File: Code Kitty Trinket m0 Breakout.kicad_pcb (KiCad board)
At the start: 2 copper layers, 39.6 x 39.6 mm, 9 parts, among them J1 Power, J2 Touch, P1 Left Servo, P2 Right Servo, P3 Sensor

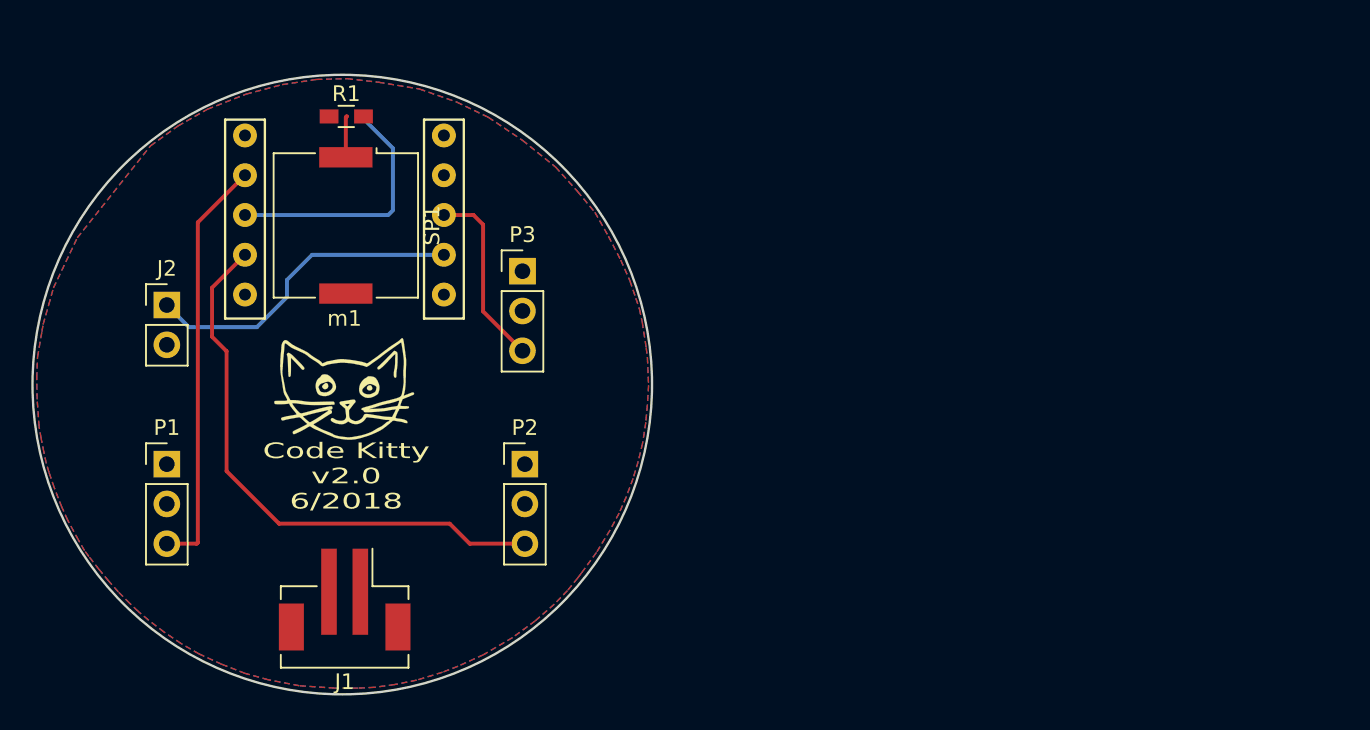
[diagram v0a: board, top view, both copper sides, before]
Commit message: Version 2.1 redesign
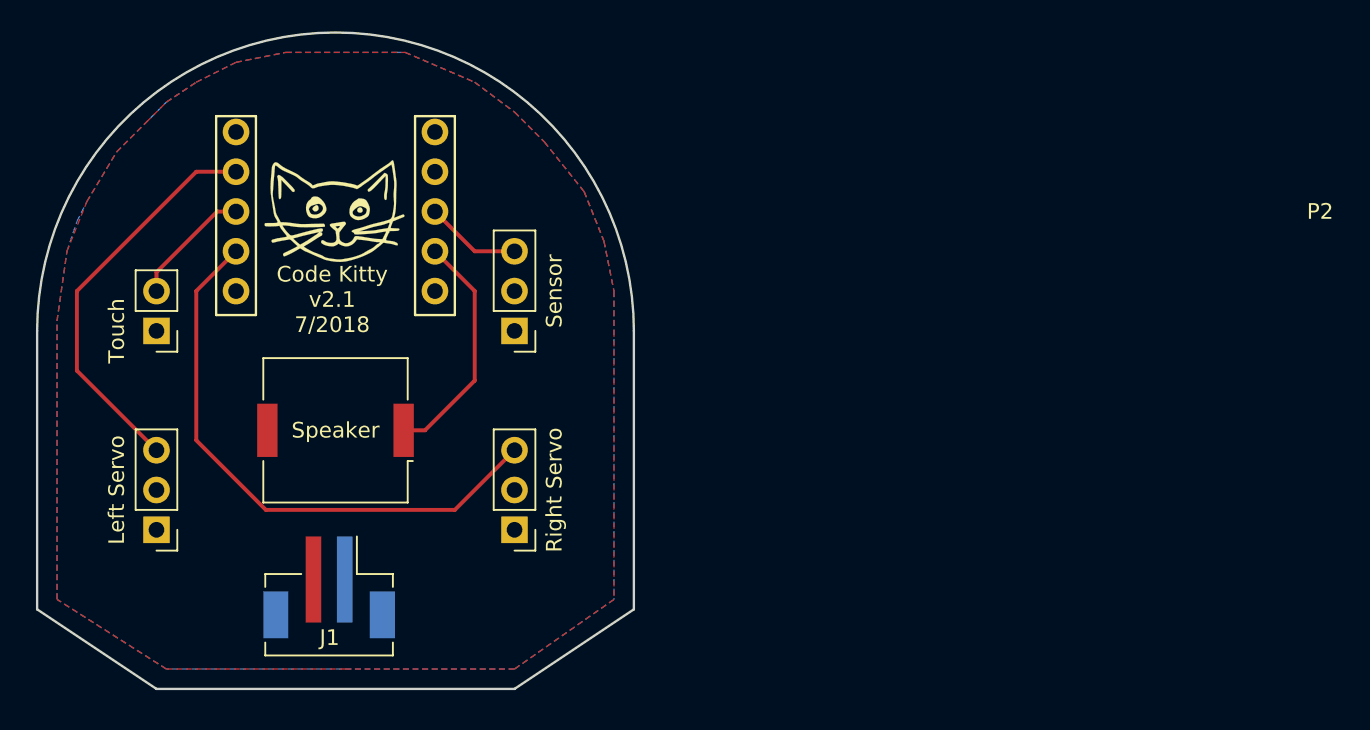
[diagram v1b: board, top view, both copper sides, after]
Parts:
- removed R1: 1K, Resistors_SMD:R_0603_HandSoldering
- m1: value (none) -> Trinket-m0
- moved Speaker 13.1 mm to (156.2, 133.3), turned to 180 degrees
- moved G*** 11.4 mm to (156.0, 119.4)
- moved P1 4.24 mm to (144.8, 139.7), turned to 180 degrees
- moved P2 4.24 mm to (167.6, 139.7), turned to 180 degrees
- moved P3 3.84 mm to (167.6, 127.0), turned to 180 degrees
- moved P4 1.78 mm to (144.8, 127.0), turned to 180 degrees
- moved J1 1.26 mm to (155.8, 144.0)
- moved m1 0.61 mm to (148.6, 105.7)
- renumbered J2 to P4, SP1 to Speaker
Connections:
- J1 pad : (no net) -> GND
- J1 pad 1: VCC -> GND
- J1 pad 2: GND -> VCC
- P4 pad 1: Touch -> GND
- P4 pad 2: GND -> Touch
- Speaker pad 1: Net-(R1-Pad1) -> BUZZ
- m1 pad 10: Net-(m1-Pad10) -> (no net)
- m1 pad 4: Touch -> BUZZ
- m1 pad 5: Net-(m1-Pad5) -> (no net)
- m1 pad 6: Net-(m1-Pad6) -> VCC
- m1 pad 8: BUZZ -> Touch
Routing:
- net Touch: track 21.4 -> 7.89 mm
- net SENS: track 11.9 -> 6.13 mm
- net Net-(R1-Pad1): track 2.66 -> 0.00 mm
- net LSERVO: track 26.7 -> 25.6 mm
- net BUZZ: track 16.1 -> 15.2 mm
- net RSERVO: track 36.0 -> 36.9 mm
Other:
- board size 39.6 x 39.6 mm -> 38.1 x 41.9 mm
- rule pad_to_mask_clearance: 0.2 -> 0.0508
- board text added: "Code Kitty v2.1 7/2018"
- board text added: "Left Servo"
- board text added: "Right Servo"
- board text added: "Sensor"
- board text added: "Touch"
- board text removed: "Code Kitty v2.0 6/2018"

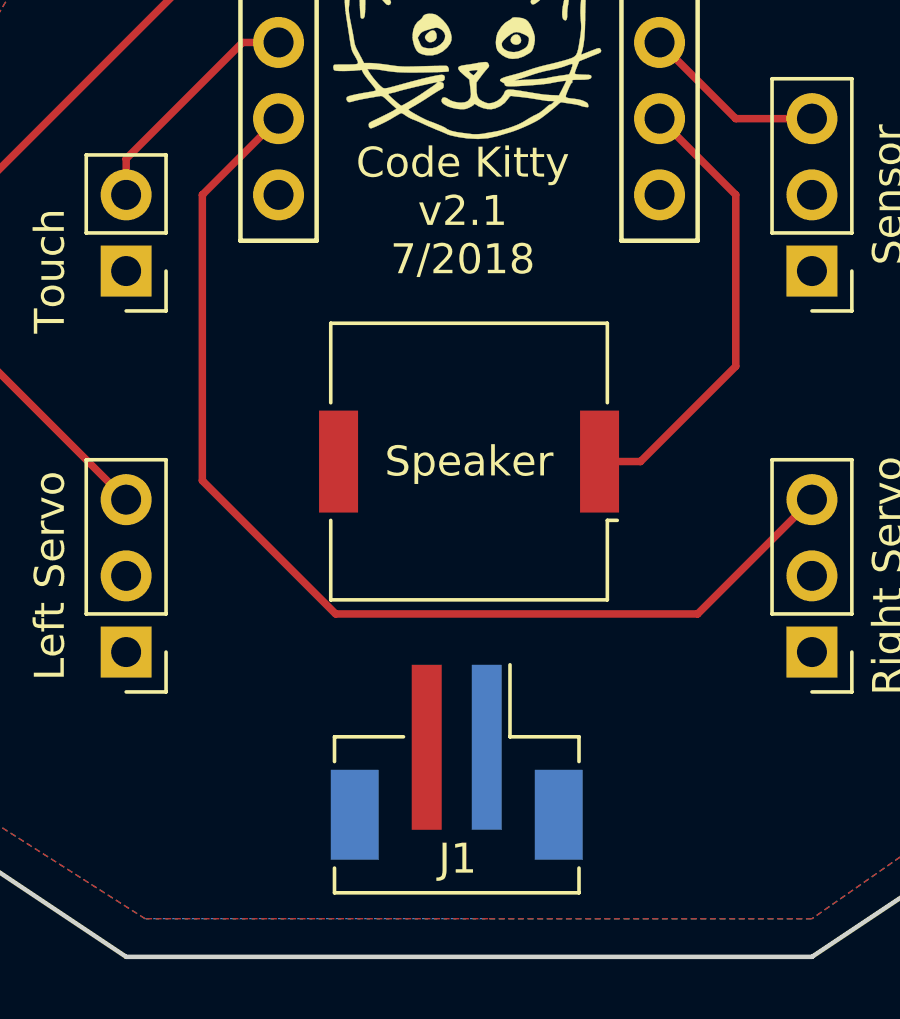
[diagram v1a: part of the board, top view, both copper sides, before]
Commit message: added ground vias for JST connector and Speaker
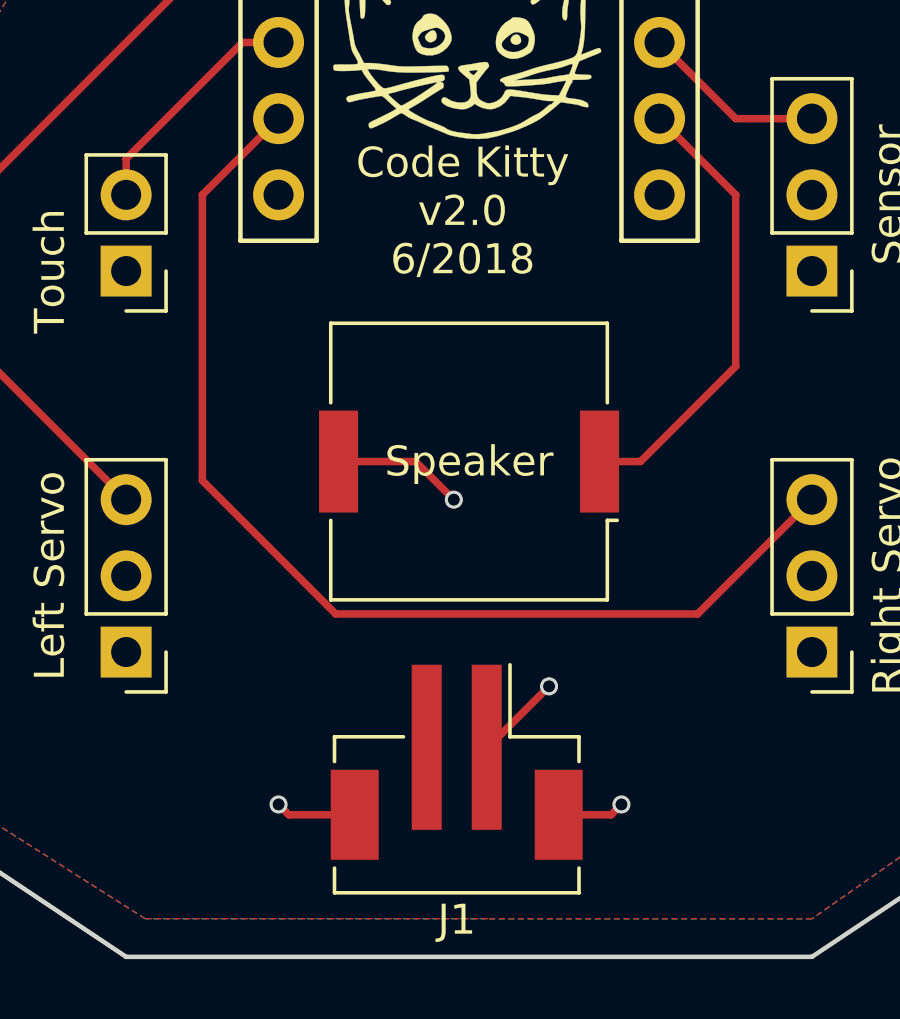
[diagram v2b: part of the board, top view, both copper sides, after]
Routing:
- net GND: track 0.00 -> 12.2 mm, vias 0 -> 4
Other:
- board text added: "Code Kitty v2.0 6/2018"
- board text removed: "Code Kitty v2.1 7/2018"
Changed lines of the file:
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@@
   (general
     (links 18)
-    (no_connects 1)
+    (no_connects 0)
     (area 137.084999 105.22 220.251191 149.935001)
     (thickness 1.6)
     (drawings 11)
-    (tracks 19)
+    (tracks 31)
     (zones 0)
     (modules 8)
@@
   (layers
     (0 F.Cu signal)
-    (31 B.Cu signal)
+    (31 B.Cu signal hide)
     (32 B.Adhes user)
     (33 F.Adhes user)
@@
   (setup
     (last_trace_width 0.25)
+    (user_trace_width 0.5)
     (trace_clearance 0.2)
     (zone_clearance 0.508)
@@
     (add_net Touch)
     (add_net VCC)
-  )
-  (module Connectors_JST:JST_PH_B2B-PH-SM4-TB_02x2.00mm_Straight (layer F.Cu)
-    (at 155.8 144 180)
-    (descr "JST PH series connector, B2B-PH-SM4-TB, top entry type, surface mount, Datasheet: http://www.jst-mfg.com/product/pdf/eng/ePH.pdf")
-    (tags "connector jst ph")
-    (attr smd)
-    (fp_text reference J1 (at -0.03 -2.59 180) (layer F.SilkS)
-      (effects (font (size 1 1) (thickness 0.15)))
-    )
-    (fp_text value Power (at 0 4.875 180) (layer F.Fab)
-      (effects (font (size 1 1) (thickness 0.15)))
-    )
-    (fp_line (start -4.075 -2.9) (end -4.075 -3.725) (layer F.SilkS) (width 0.12))
-    (fp_line (start -4.075 -3.725) (end 4.075 -3.725) (layer F.SilkS) (width 0.12))
-    (fp_line (start 4.075 -3.725) (end 4.075 -2.9) (layer F.SilkS) (width 0.12))
-    (fp_line (start -4.075 0.65) (end -4.075 1.475) (layer F.SilkS) (width 0.12))
-    (fp_line (start -4.075 1.475) (end -1.775 1.475) (layer F.SilkS) (width 0.12))
-    (fp_line (start 4.075 0.65) (end 4.075 1.475) (layer F.SilkS) (width 0.12))
-    (fp_line (start 4.075 1.475) (end 1.775 1.475) (layer F.SilkS) (width 0.12))
-    (fp_line (start -3.975 -3.625) (end -3.975 1.375) (layer F.Fab) (width 0.1))
-    (fp_line (start -3.975 1.375) (end 3.975 1.375) (layer F.Fab) (width 0.1))
-    (fp_line (start 3.975 1.375) (end 3.975 -3.625) (layer F.Fab) (width 0.1))
-    (fp_line (start 3.975 -3.625) (end -3.975 -3.625) (layer F.Fab) (width 0.1))
-    (fp_line (start -1.775 1.475) (end -1.775 3.875) (layer F.SilkS) (width 0.12))
-    (fp_line (start -2 1.375) (end -1 0.375) (layer F.Fab) (width 0.1))
-    (fp_line (start -1 0.375) (end 0 1.375) (layer F.Fab) (width 0.1))
-    (fp_line (start -4.7 -4.13) (end -4.7 4.38) (layer F.CrtYd) (width 0.05))
-    (fp_line (start -4.7 4.38) (end 4.7 4.38) (layer F.CrtYd) (width 0.05))
-    (fp_line (start 4.7 4.38) (end 4.7 -4.13) (layer F.CrtYd) (width 0.05))
-    (fp_line (start 4.7 -4.13) (end -4.7 -4.13) (layer F.CrtYd) (width 0.05))
-    (fp_text user %R (at 0 -2.625 180) (layer F.Fab)
-      (effects (font (size 1 1) (thickness 0.15)))
-    )
-    (pad 1 smd rect (at -1 1.125 180) (size 1 5.5) (layers B.Cu F.Paste F.Mask)
-      (net 2 GND))
-    (pad 2 smd rect (at 1 1.125 180) (size 1 5.5) (layers F.Cu F.Paste F.Mask)
-      (net 1 VCC))
-    (pad "" smd rect (at -3.4 -1.125 180) (size 1.6 3) (layers B.Cu F.Paste F.Mask)
-      (net 2 GND))
-    (pad "" smd rect (at 3.4 -1.125 180) (size 1.6 3) (layers B.Cu F.Paste F.Mask)
-      (net 2 GND))
-    (model ${KISYS3DMOD}/Connectors_JST.3dshapes/JST_PH_B2B-PH-SM4-TB_02x2.00mm_Straight.wrl
-      (at (xyz 0 0 0))
-      (scale (xyz 1 1 1))
-      (rotate (xyz 0 0 0))
-    )
   )
   (module Buzzers_Beepers:Buzzer_Murata_PKMCS0909E4000-R1 (layer F.Cu)
@@
       (xy -1.172602 -0.309545) (xy -1.077038 -0.381913) (xy -0.997162 -0.406855) (xy -0.934043 -0.384502)) (layer F.SilkS) (width 0.01))
   )
+  (module Connectors_JST:JST_PH_B2B-PH-SM4-TB_02x2.00mm_Straight (layer F.Cu)
+    (at 155.8 144 180)
+    (descr "JST PH series connector, B2B-PH-SM4-TB, top entry type, surface mount, Datasheet: http://www.jst-mfg.com/product/pdf/eng/ePH.pdf")
+    (tags "connector jst ph")
+    (attr smd)
+    (fp_text reference J1 (at 0 -4.625 180) (layer F.SilkS)
+      (effects (font (size 1 1) (thickness 0.15)))
+    )
+    (fp_text value Power (at 0 4.875 180) (layer F.Fab)
+      (effects (font (size 1 1) (thickness 0.15)))
+    )
+    (fp_line (start -4.075 -2.9) (end -4.075 -3.725) (layer F.SilkS) (width 0.12))
+    (fp_line (start -4.075 -3.725) (end 4.075 -3.725) (layer F.SilkS) (width 0.12))
+    (fp_line (start 4.075 -3.725) (end 4.075 -2.9) (layer F.SilkS) (width 0.12))
+    (fp_line (start -4.075 0.65) (end -4.075 1.475) (layer F.SilkS) (width 0.12))
+    (fp_line (start -4.075 1.475) (end -1.775 1.475) (layer F.SilkS) (width 0.12))
+    (fp_line (start 4.075 0.65) (end 4.075 1.475) (layer F.SilkS) (width 0.12))
+    (fp_line (start 4.075 1.475) (end 1.775 1.475) (layer F.SilkS) (width 0.12))
+    (fp_line (start -3.975 -3.625) (end -3.975 1.375) (layer F.Fab) (width 0.1))
+    (fp_line (start -3.975 1.375) (end 3.975 1.375) (layer F.Fab) (width 0.1))
+    (fp_line (start 3.975 1.375) (end 3.975 -3.625) (layer F.Fab) (width 0.1))
+    (fp_line (start 3.975 -3.625) (end -3.975 -3.625) (layer F.Fab) (width 0.1))
+    (fp_line (start -1.775 1.475) (end -1.775 3.875) (layer F.SilkS) (width 0.12))
+    (fp_line (start -2 1.375) (end -1 0.375) (layer F.Fab) (width 0.1))
+    (fp_line (start -1 0.375) (end 0 1.375) (layer F.Fab) (width 0.1))
+    (fp_line (start -4.7 -4.13) (end -4.7 4.38) (layer F.CrtYd) (width 0.05))
+    (fp_line (start -4.7 4.38) (end 4.7 4.38) (layer F.CrtYd) (width 0.05))
+    (fp_line (start 4.7 4.38) (end 4.7 -4.13) (layer F.CrtYd) (width 0.05))
+    (fp_line (start 4.7 -4.13) (end -4.7 -4.13) (layer F.CrtYd) (width 0.05))
+    (fp_text user %R (at 0 -2.625 180) (layer F.Fab)
+      (effects (font (size 1 1) (thickness 0.15)))
+    )
+    (pad 1 smd rect (at -1 1.125 180) (size 1 5.5) (layers F.Cu F.Paste F.Mask)
+      (net 2 GND))
+    (pad 2 smd rect (at 1 1.125 180) (size 1 5.5) (layers F.Cu F.Paste F.Mask)
+      (net 1 VCC))
+    (pad "" smd rect (at -3.4 -1.125 180) (size 1.6 3) (layers F.Cu F.Paste F.Mask)
+      (net 2 GND))
+    (pad "" smd rect (at 3.4 -1.125 180) (size 1.6 3) (layers F.Cu F.Paste F.Mask)
+      (net 2 GND))
+    (model ${KISYS3DMOD}/Connectors_JST.3dshapes/JST_PH_B2B-PH-SM4-TB_02x2.00mm_Straight.wrl
+      (at (xyz 0 0 0))
+      (scale (xyz 1 1 1))
+      (rotate (xyz 0 0 0))
+    )
+  )
   (gr_line (start 144.78 149.86) (end 137.16 144.78) (layer Edge.Cuts) (width 0.15))
   (gr_line (start 167.64 149.86) (end 144.78 149.86) (layer Edge.Cuts) (width 0.15))
@@
     (effects (font (size 1 1) (thickness 0.25)))
   )
-  (gr_text "Code Kitty\nv2.1\n7/2018" (at 156 125) (layer F.SilkS)
+  (gr_text "Code Kitty\nv2.0\n6/2018" (at 156 125) (layer F.SilkS)
     (effects (font (size 1 1) (thickness 0.1)))
   )
   (segment (start 163.1315 114.5226) (end 163.2144 114.5226) (width 0.25) (layer F.Cu) (net 1) (status 30))
+  (segment (start 151.86 133.35) (end 154.432 133.35) (width 0.25) (layer F.Cu) (net 2) (status 400000))
+  (via (at 155.702 134.62) (size 0.6) (drill 0.4) (layers F.Cu B.Cu) (net 2))
+  (segment (start 154.432 133.35) (end 155.702 134.62) (width 0.25) (layer F.Cu) (net 2))
+  (via (at 158.877 140.843) (size 0.6) (drill 0.4) (layers F.Cu B.Cu) (net 2))
+  (segment (start 156.845 142.875) (end 158.877 140.843) (width 0.25) (layer F.Cu) (net 2) (status 400000))
+  (segment (start 156.8 142.875) (end 156.845 142.875) (width 0.25) (layer F.Cu) (net 2) (status C00000))
+  (segment (start 159.2 145.125) (end 160.945 145.125) (width 0.25) (layer F.Cu) (net 2) (status 400000))
+  (via (at 161.29 144.78) (size 0.6) (drill 0.4) (layers F.Cu B.Cu) (net 2))
+  (segment (start 160.945 145.125) (end 161.29 144.78) (width 0.25) (layer F.Cu) (net 2))
+  (segment (start 152.4 145.125) (end 150.205 145.125) (width 0.25) (layer F.Cu) (net 2) (status 400000))
+  (via (at 149.86 144.78) (size 0.6) (drill 0.4) (layers F.Cu B.Cu) (net 2))
+  (segment (start 150.205 145.125) (end 149.86 144.78) (width 0.25) (layer F.Cu) (net 2))
   (segment (start 149.86 119.38) (end 148.657919 119.38) (width 0.25) (layer F.Cu) (net 3))
   (segment (start 148.657919 119.38) (end 144.78 123.257919) (width 0.25) (layer F.Cu) (net 3))

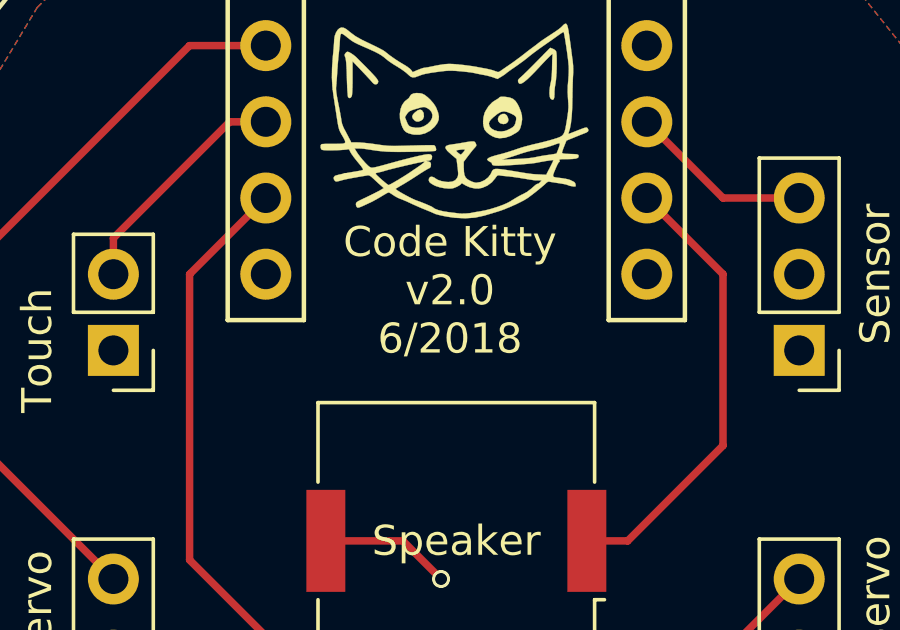
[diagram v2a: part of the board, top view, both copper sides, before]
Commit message: Fixed text on board to say Code Kitty 2.2
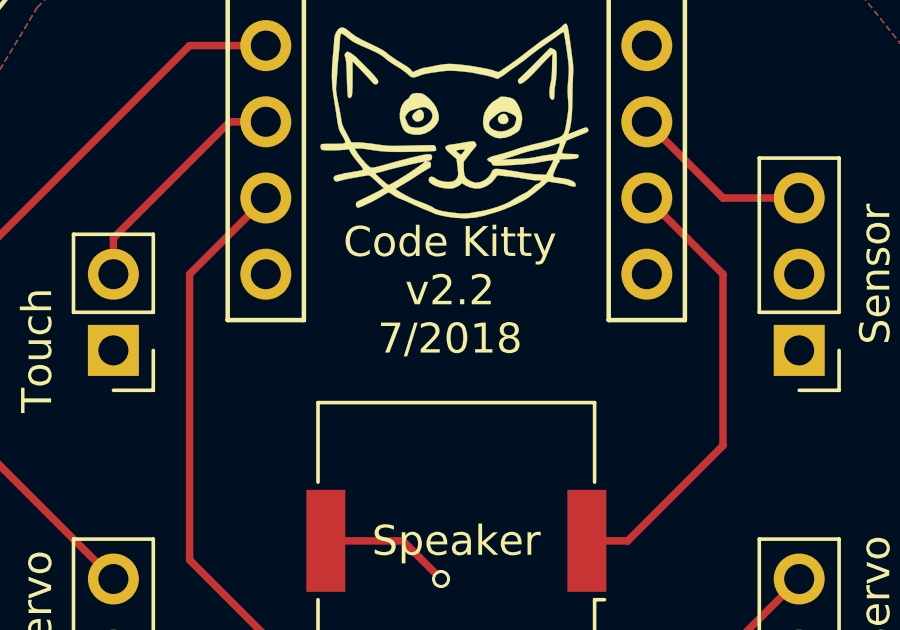
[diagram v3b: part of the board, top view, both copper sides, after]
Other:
- board text added: "Code Kitty v2.2 7/2018"
- board text removed: "Code Kitty v2.0 6/2018"
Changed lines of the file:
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@@
     (links 18)
     (no_connects 0)
-    (area 137.084999 105.22 220.251191 149.935001)
+    (area 137.084999 107.874999 175.335001 149.935001)
     (thickness 1.6)
     (drawings 11)
@@
     (effects (font (size 1 1) (thickness 0.25)))
   )
-  (gr_text "Code Kitty\nv2.0\n6/2018" (at 156 125) (layer F.SilkS)
+  (gr_text "Code Kitty\nv2.2\n7/2018" (at 156 125) (layer F.SilkS)
     (effects (font (size 1 1) (thickness 0.1)))
   )
   (segment (start 163.1315 114.5226) (end 163.2144 114.5226) (width 0.25) (layer F.Cu) (net 1) (status 30))
-  (segment (start 151.86 133.35) (end 154.432 133.35) (width 0.25) (layer F.Cu) (net 2) (status 400000))
+  (segment (start 151.86 133.35) (end 154.432 133.35) (width 0.25) (layer F.Cu) (net 2))
   (via (at 155.702 134.62) (size 0.6) (drill 0.4) (layers F.Cu B.Cu) (net 2))
   (segment (start 154.432 133.35) (end 155.702 134.62) (width 0.25) (layer F.Cu) (net 2))
   (via (at 158.877 140.843) (size 0.6) (drill 0.4) (layers F.Cu B.Cu) (net 2))
-  (segment (start 156.845 142.875) (end 158.877 140.843) (width 0.25) (layer F.Cu) (net 2) (status 400000))
-  (segment (start 156.8 142.875) (end 156.845 142.875) (width 0.25) (layer F.Cu) (net 2) (status C00000))
-  (segment (start 159.2 145.125) (end 160.945 145.125) (width 0.25) (layer F.Cu) (net 2) (status 400000))
+  (segment (start 156.845 142.875) (end 158.877 140.843) (width 0.25) (layer F.Cu) (net 2))
+  (segment (start 156.8 142.875) (end 156.845 142.875) (width 0.25) (layer F.Cu) (net 2))
+  (segment (start 159.2 145.125) (end 160.945 145.125) (width 0.25) (layer F.Cu) (net 2))
   (via (at 161.29 144.78) (size 0.6) (drill 0.4) (layers F.Cu B.Cu) (net 2))
   (segment (start 160.945 145.125) (end 161.29 144.78) (width 0.25) (layer F.Cu) (net 2))
-  (segment (start 152.4 145.125) (end 150.205 145.125) (width 0.25) (layer F.Cu) (net 2) (status 400000))
+  (segment (start 152.4 145.125) (end 150.205 145.125) (width 0.25) (layer F.Cu) (net 2))
   (via (at 149.86 144.78) (size 0.6) (drill 0.4) (layers F.Cu B.Cu) (net 2))
   (segment (start 150.205 145.125) (end 149.86 144.78) (width 0.25) (layer F.Cu) (net 2))
